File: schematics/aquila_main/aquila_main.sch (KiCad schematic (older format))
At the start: 26 parts, among them IC1 TPS62152, IC2 TPS62132

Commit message: added symbol and footprint for ADXL357
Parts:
- removed IC?: ADXL357, cusf:ADXL3x5, symbol cusf-kicad:ADXL375
- added U?: ADXL357, symbol aquila:ADXL357
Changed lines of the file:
@@
-$EndComp
-$Comp
-L cusf-kicad:ADXL375 IC?
-U 1 1 62148246
-P 6700 1700
-F 0 "IC?" H 6700 2225 50  0000 C CNN
-F 1 "ADXL357" H 6700 2134 50  0000 C CNN
-F 2 "cusf:ADXL3x5" H 6400 1000 50  0001 L CNN
-F 3 "" H 6300 1200 50  0001 C CNN
-F 4 "2361527" H 6400 900 50  0001 L CNN "Farnell"
-	1    6700 1700
-	1    0    0    -1
 $EndComp
 $Comp
@@
 Wire Wire Line
 	12700 4400 13150 4400
+$Comp
+L aquila:ADXL357 U?
+U 1 1 625041A3
+P 6600 1450
+F 0 "U?" H 6600 1475 50  0000 C CNN
+F 1 "ADXL357" H 6600 1384 50  0000 C CNN
+F 2 "" H 6600 1450 50  0001 C CNN
+F 3 "" H 6600 1450 50  0001 C CNN
+	1    6600 1450
+	1    0    0    -1
+$EndComp
 $EndSCHEMATC

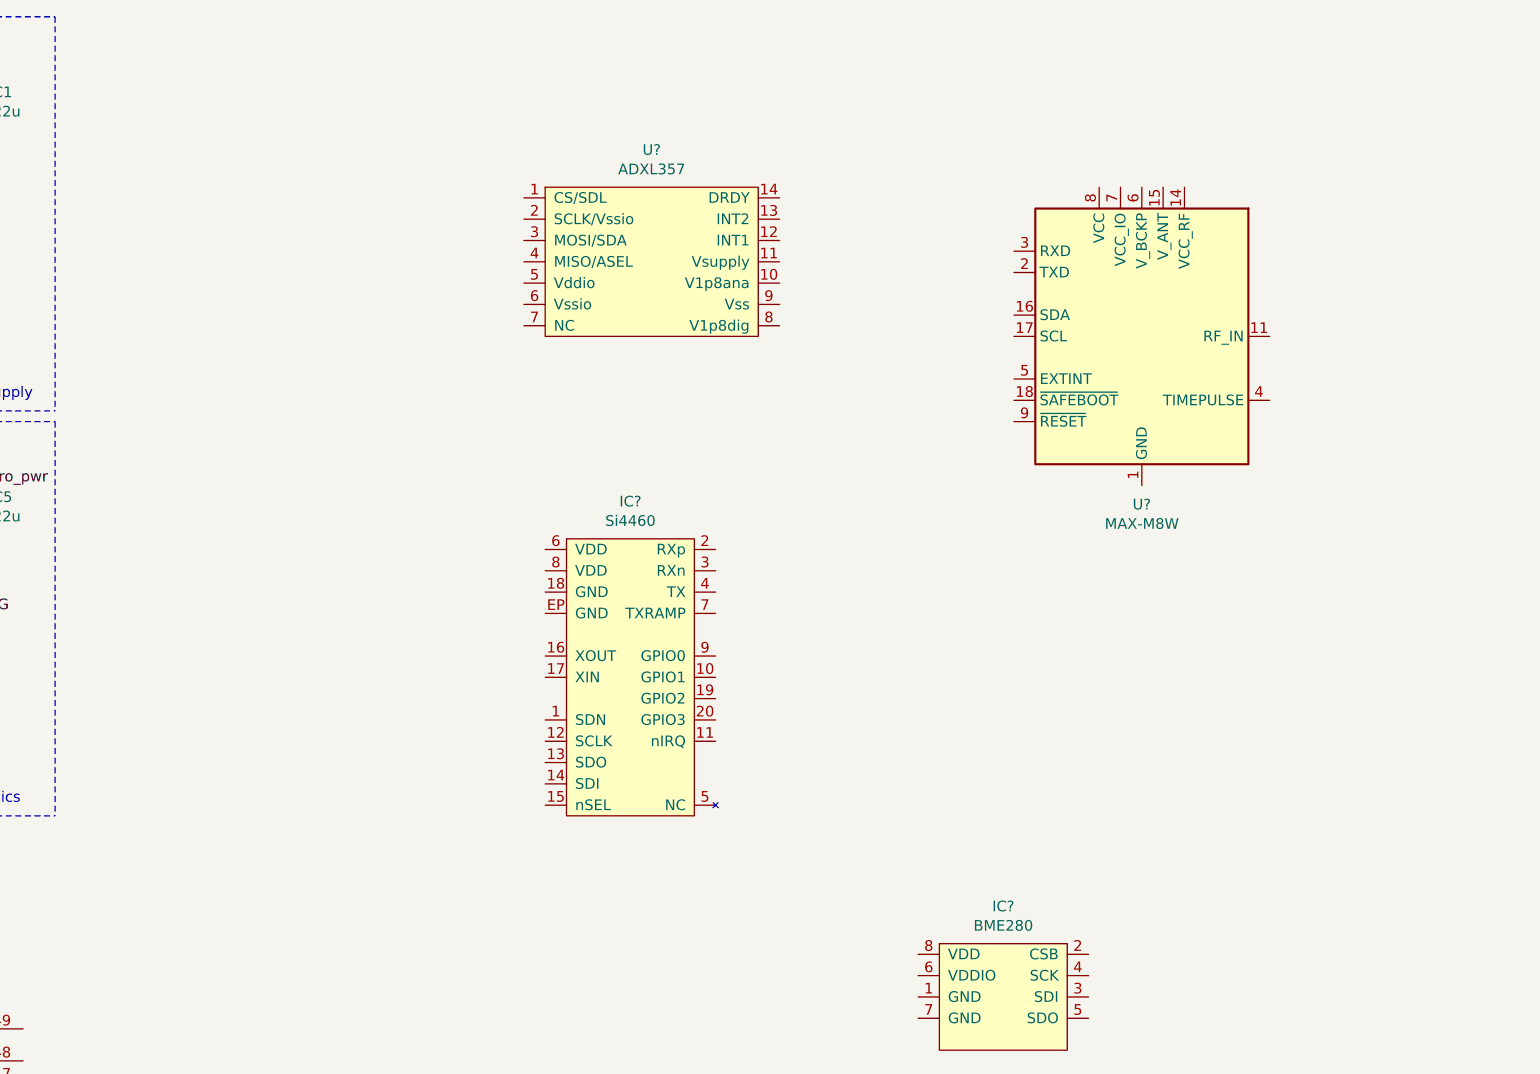
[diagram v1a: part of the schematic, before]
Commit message: added connections for accelerometer
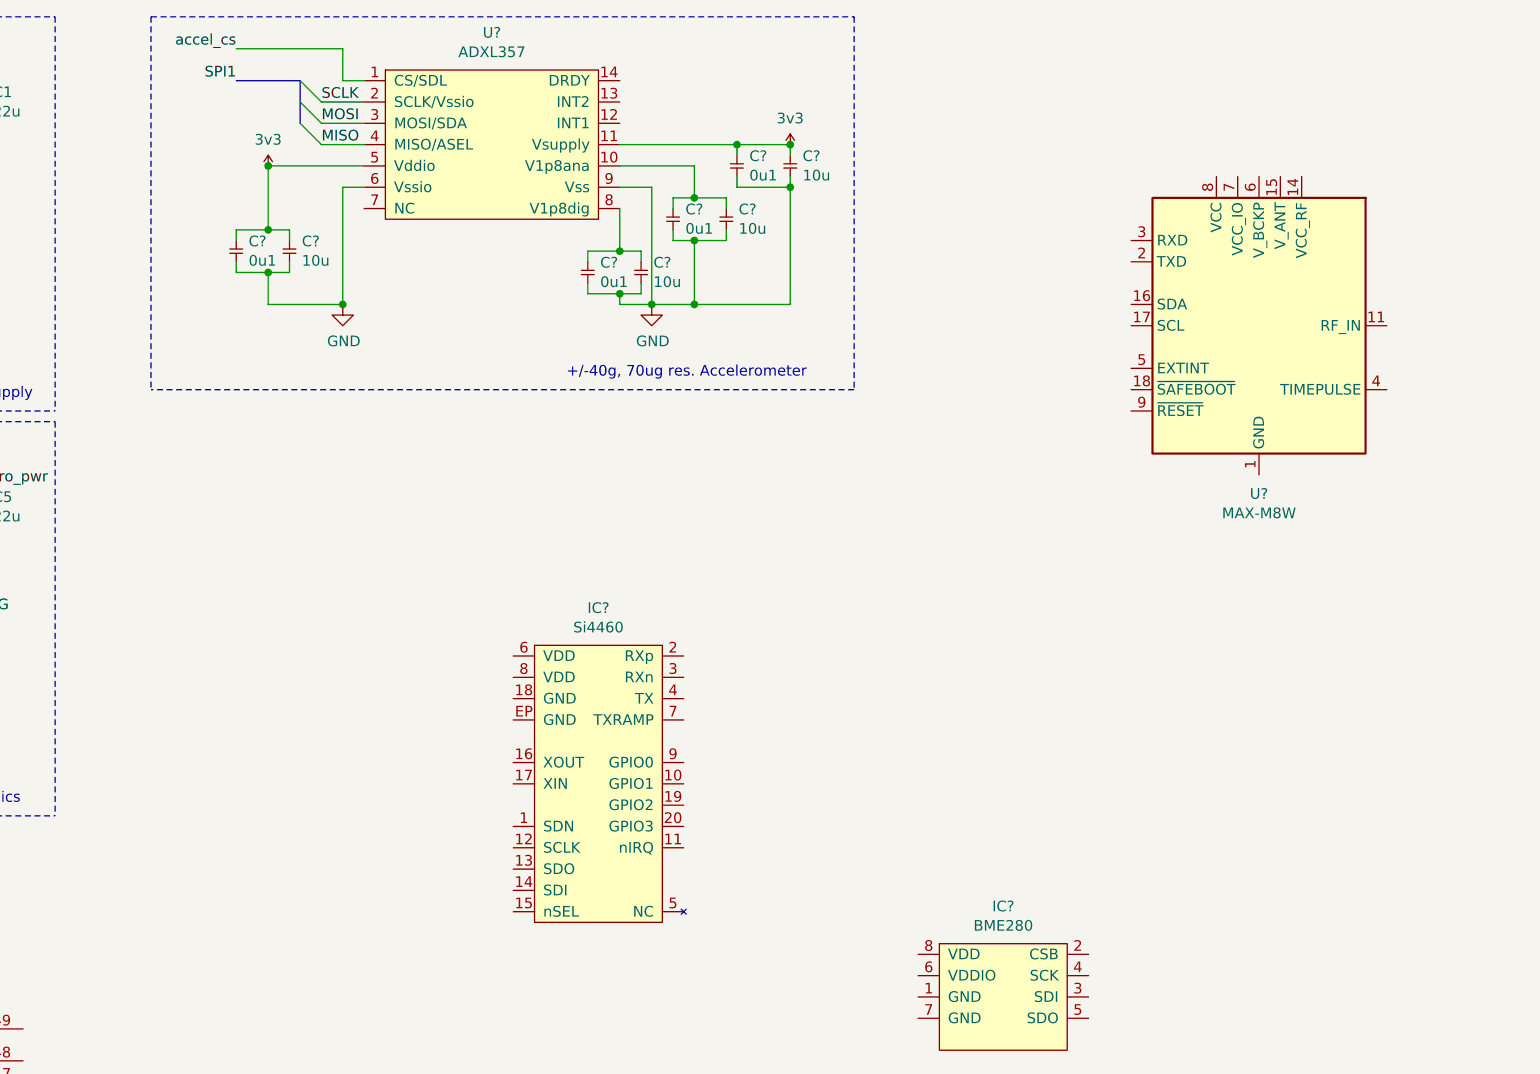
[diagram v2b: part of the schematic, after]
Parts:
- added C? (x4): 10u, symbol cusf-kicad:C
- added C? (x4): 0u1, symbol cusf-kicad:C
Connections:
- net 3v3: now also U?.11 (Vsupply), U?.5 (Vddio), C?.1, C?.1, C?.1, C?.1
- net GND: now also U?.6 (Vssio), U?.9 (Vss), C?.2, C?.2, C?.2, C?.2, C?.2, C?.2, C?.2, C?.2
- net accel_cs: now reaches U?.1 (CS/SDL)
- net at U?.10 (V1p8ana): now also C?.1, C?.1
- net SCLK: now reaches U?.2 (SCLK/Vssio)
- net MOSI: now reaches U?.3 (MOSI/SDA)
- net MISO: now reaches U?.4 (MISO/ASEL)
- net at U?.8 (V1p8dig): now also C?.1, C?.1
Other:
- note added: "+/-40g, 70ug res. Accelerometer"
- moved on the sheet: IC?, U?

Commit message: added symbol and footprint for RTC bat. holder
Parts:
- removed IC?: Si4460, cusf:QFN-20-EP-SI, symbol cusf-kicad:Si4460
- added J?: 120591-1, symbol aquila:120591-1
- added U?: Si4463, Package_DFN_QFN:QFN-20-1EP_4x4mm_P0.5mm_EP2.6x2.6mm_ThermalVias, symbol RF:Si4463
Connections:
- net GND: now also J?.2 (-), U?.18 (GND), U?.21 (GND)
- net accel_drdy: now reaches U?.14 (DRDY)
- new net vbat: J?.1 (+)
- no-connect marks 0 -> 3
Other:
- note added: "3V CR2032 for Real Time Clock"
- moved on the sheet: U?
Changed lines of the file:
@@
 L teensy:Teensy4.1 U?
 U 1 1 62144D72
-P 2550 7850
-F 0 "U?" H 2550 10415 50  0000 C CNN
-F 1 "Teensy4.1" H 2550 10324 50  0000 C CNN
-F 2 "" H 2150 8250 50  0001 C CNN
-F 3 "" H 2150 8250 50  0001 C CNN
-	1    2550 7850
-	1    0    0    -1
-$EndComp
-$Comp
-L cusf-kicad:Si4460 IC?
-U 1 1 62148F07
-P 6350 4400
-F 0 "IC?" H 6350 5225 50  0000 C CNN
-F 1 "Si4460" H 6350 5134 50  0000 C CNN
-F 2 "cusf:QFN-20-EP-SI" H 6050 3600 50  0001 L CNN
-F 3 "" H 5950 5000 50  0001 C CNN
-F 4 "2462635" H 6050 3500 50  0001 L CNN "Farnell"
-	1    6350 4400
+P 2750 9200
+F 0 "U?" H 2750 11765 50  0000 C CNN
+F 1 "Teensy4.1" H 2750 11674 50  0000 C CNN
+F 2 "" H 2350 9600 50  0001 C CNN
+F 3 "" H 2350 9600 50  0001 C CNN
+	1    2750 9200
 	1    0    0    -1
 $EndComp
@@
 Wire Notes Line
 	4250 800  4250 2550
+NoConn ~ 5250 1700
+NoConn ~ 6450 1200
+NoConn ~ 6450 1300
+Text Label 6700 1100 0    50   ~ 0
+accel_drdy
+Wire Wire Line
+	6450 1100 6700 1100
+$Comp
+L RF:Si4463 U?
+U 1 1 6268F7FD
+P 5300 4400
+F 0 "U?" H 5300 5400 50  0000 C CNN
+F 1 "Si4463" H 5300 5300 50  0000 C CNN
+F 2 "Package_DFN_QFN:QFN-20-1EP_4x4mm_P0.5mm_EP2.6x2.6mm_ThermalVias" H 5300 5600 50  0001 C CNN
+F 3 "https://www.silabs.com/documents/public/data-sheets/Si4464-63-61-60.pdf" H 5000 4300 50  0001 C CNN
+	1    5300 4400
+	1    0    0    -1
+$EndComp
+$Comp
+L aquila:120591-1 J?
+U 1 1 626A7BFD
+P 1550 4650
+F 0 "J?" H 1678 4526 50  0000 L CNN
+F 1 "120591-1" H 1678 4435 50  0000 L CNN
+F 2 "" H 1550 4800 50  0001 C CNN
+F 3 "" H 1550 4800 50  0001 C CNN
+	1    1550 4650
+	1    0    0    -1
+$EndComp
+Wire Wire Line
+	1400 4900 1400 5000
+$Comp
+L power:GND #PWR?
+U 1 1 626ADD67
+P 1400 5000
+F 0 "#PWR?" H 1400 4750 50  0001 C CNN
+F 1 "GND" H 1405 4827 50  0000 C CNN
+F 2 "" H 1400 5000 50  0001 C CNN
+F 3 "" H 1400 5000 50  0001 C CNN
+	1    1400 5000
+	1    0    0    -1
+$EndComp
+Text Label 1250 4750 2    50   ~ 0
+vbat
+Wire Wire Line
+	1250 4750 1400 4750
+Wire Notes Line
+	1000 4600 3800 4600
+Wire Notes Line
+	1000 5300 3800 5300
+Wire Notes Line
+	1000 4600 1000 5300
+Wire Notes Line
+	3800 4600 3800 5300
 Wire Bus Line
 	4950 1100 4950 1300
+Text Notes 2550 5250 0    50   ~ 0
+3V CR2032 for Real Time Clock
 $EndSCHEMATC

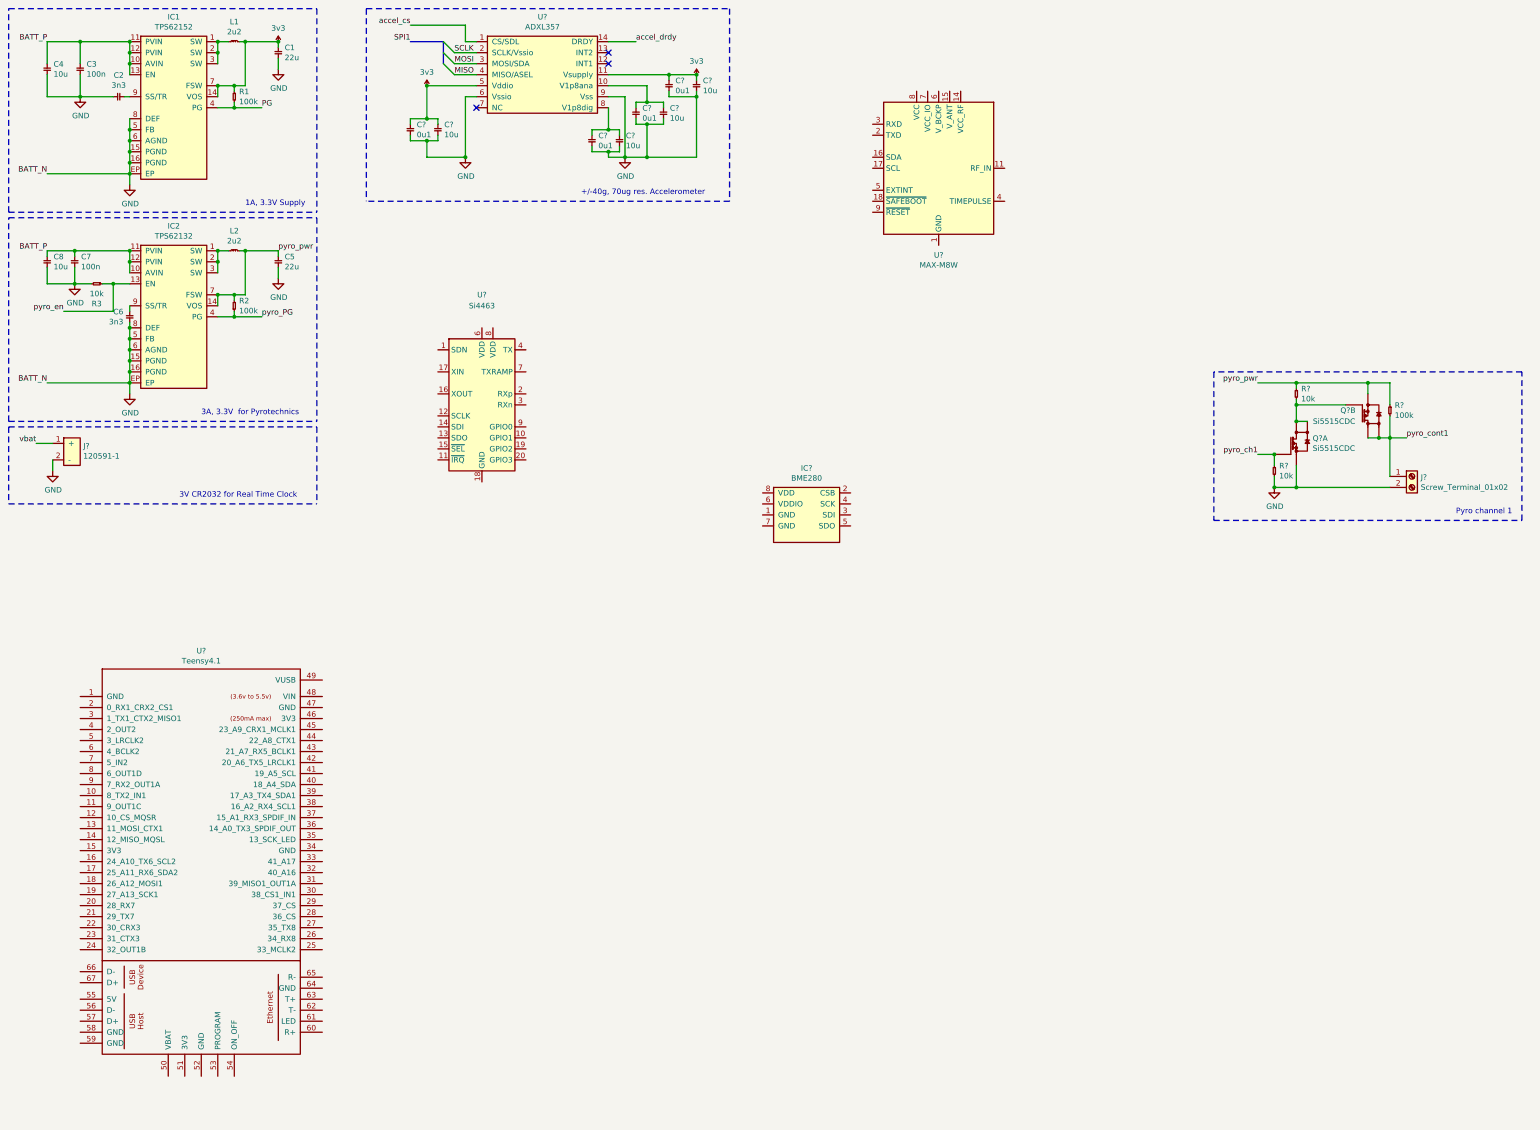
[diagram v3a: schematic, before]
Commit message: added connections for barometer
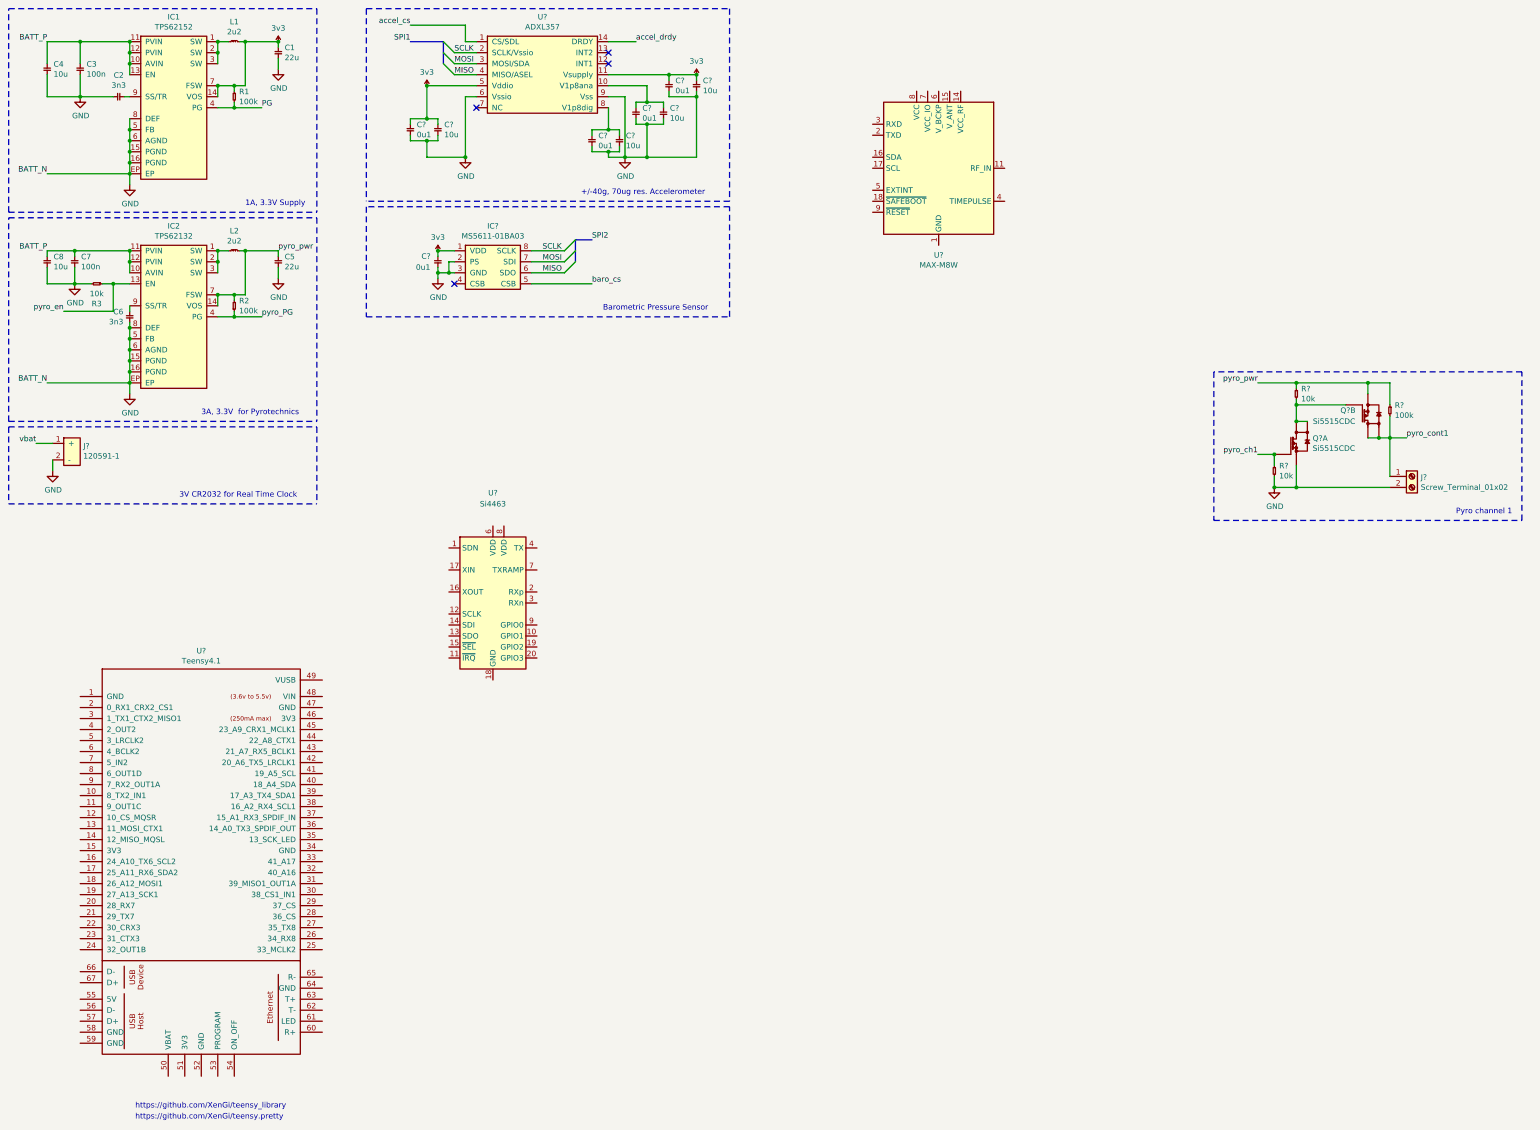
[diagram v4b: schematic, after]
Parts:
- removed IC?: BME280, cusf:BME280, symbol cusf-kicad:BME280
- added C?: 0u1, symbol cusf-kicad:C
- added IC?: MS5611-01BA03, cusf:MS5611, symbol cusf-kicad:MS5611-01BA03
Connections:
- net 3v3: now also C?.1, IC?.1 (VDD)
- net GND: now also C?.2, IC?.2 (PS), IC?.3 (GND)
- net MISO: now also IC?.6 (SDO)
- net MOSI: now also IC?.7 (SDI)
- net SCLK: now also IC?.8 (SCLK)
- new net baro_cs: IC?.5 (CSB)
- no-connect marks 3 -> 4
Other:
- note added: "Barometric Pressure Sensor"
- note added: "https://github.com/XenGi/teensy.pretty"
- note added: "https://github.com/XenGi/teensy_library"
- moved on the sheet: U?
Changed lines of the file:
@@
 	2100 2300 1350 2300
-$Comp
-L cusf-kicad:BME280 IC?
-U 1 1 621D3869
-P 8250 5400
-F 0 "IC?" H 8250 5825 50  0000 C CNN
-F 1 "BME280" H 8250 5734 50  0000 C CNN
-F 2 "cusf:BME280" H 7950 5000 50  0001 L CNN
-F 3 "https://ae-bst.resource.bosch.com/media/_tech/media/datasheets/BST-BME280_DS001-11.pdf" H 7950 4900 50  0001 L CNN
-F 4 "262-BME280" H 7950 4800 50  0001 L CNN "Mouser"
-F 5 "828-1063-1-ND" H 7950 4700 50  0001 L CNN "Digi-Key"
-	1    8250 5400
-	1    0    0    -1
-$EndComp
 $Comp
 L cusf-kicad:3v3 #PWR?
@@
 L RF:Si4463 U?
 U 1 1 6268F7FD
-P 5300 4400
-F 0 "U?" H 5300 5400 50  0000 C CNN
-F 1 "Si4463" H 5300 5300 50  0000 C CNN
-F 2 "Package_DFN_QFN:QFN-20-1EP_4x4mm_P0.5mm_EP2.6x2.6mm_ThermalVias" H 5300 5600 50  0001 C CNN
-F 3 "https://www.silabs.com/documents/public/data-sheets/Si4464-63-61-60.pdf" H 5000 4300 50  0001 C CNN
-	1    5300 4400
+P 5400 6200
+F 0 "U?" H 5400 7200 50  0000 C CNN
+F 1 "Si4463" H 5400 7100 50  0000 C CNN
+F 2 "Package_DFN_QFN:QFN-20-1EP_4x4mm_P0.5mm_EP2.6x2.6mm_ThermalVias" H 5400 7400 50  0001 C CNN
+F 3 "https://www.silabs.com/documents/public/data-sheets/Si4464-63-61-60.pdf" H 5100 6100 50  0001 C CNN
+	1    5400 6200
 	1    0    0    -1
 $EndComp
@@
 F 1 "120591-1" H 1678 4435 50  0000 L CNN
 F 2 "" H 1550 4800 50  0001 C CNN
-F 3 "" H 1550 4800 50  0001 C CNN
+F 3 "https://www.farnell.com/cad/1815976.pdf" H 1550 4800 50  0001 C CNN
 	1    1550 4650
 	1    0    0    -1
@@
 Wire Notes Line
 	3800 4600 3800 5300
+Text Notes 2550 5250 0    50   ~ 0
+3V CR2032 for Real Time Clock
+Text Notes 2150 10800 0    50   ~ 0
+https://github.com/XenGi/teensy_library
+Text Notes 2150 10900 0    50   ~ 0
+https://github.com/XenGi/teensy.pretty
+$Comp
+L cusf-kicad:3v3 #PWR?
+U 1 1 622BAFBF
+P 4900 3000
+F 0 "#PWR?" H 4900 3110 50  0001 L CNN
+F 1 "3v3" H 4900 3123 50  0000 C CNN
+F 2 "" H 4900 3000 50  0001 C CNN
+F 3 "" H 4900 3000 50  0001 C CNN
+	1    4900 3000
+	1    0    0    -1
+$EndComp
+Wire Wire Line
+	5050 3000 4900 3000
+$Comp
+L cusf-kicad:MS5611-01BA03 IC?
+U 1 1 622B2C48
+P 5350 3100
+F 0 "IC?" H 5400 3425 50  0000 C CNN
+F 1 "MS5611-01BA03" H 5400 3334 50  0000 C CNN
+F 2 "cusf:MS5611" H 5150 2700 50  0001 L CNN
+F 3 "" H 5400 3100 50  0001 C CNN
+F 4 "2362662" H 5150 2600 50  0001 L CNN "Farnell"
+	1    5350 3100
+	1    0    0    -1
+$EndComp
+NoConn ~ 5050 3300
+$Comp
+L power:GND #PWR?
+U 1 1 622FE465
+P 4900 3250
+F 0 "#PWR?" H 4900 3000 50  0001 C CNN
+F 1 "GND" H 4905 3077 50  0000 C CNN
+F 2 "" H 4900 3250 50  0001 C CNN
+F 3 "" H 4900 3250 50  0001 C CNN
+	1    4900 3250
+	1    0    0    -1
+$EndComp
+Wire Wire Line
+	5050 3200 5000 3200
+Wire Wire Line
+	4900 3200 4900 3250
+Wire Wire Line
+	5050 3100 5000 3100
+Wire Wire Line
+	5000 3100 5000 3200
+Connection ~ 5000 3200
+Wire Wire Line
+	5000 3200 4900 3200
+$Comp
+L cusf-kicad:C C?
+U 1 1 62311113
+P 4900 3050
+F 0 "C?" V 4900 2900 50  0000 L CNN
+F 1 "0u1" V 5000 2850 50  0000 L CNN
+F 2 "" H 4900 3050 50  0001 C CNN
+F 3 "" H 4900 3050 50  0001 C CNN
+	1    4900 3050
+	0    1    1    0
+$EndComp
+Wire Wire Line
+	4900 3000 4900 3050
+Connection ~ 4900 3000
+Wire Wire Line
+	4900 3150 4900 3200
+Connection ~ 4900 3200
+Entry Wire Line
+	6050 3000 6150 2900
+Entry Wire Line
+	6050 3100 6150 3000
+Entry Wire Line
+	6050 3200 6150 3100
+Wire Bus Line
+	6150 2900 6300 2900
+Wire Wire Line
+	6050 3000 5750 3000
+Wire Wire Line
+	5750 3100 6050 3100
+Wire Wire Line
+	6050 3200 5750 3200
+Text Label 5850 3000 0    50   ~ 0
+SCLK
+Text Label 5850 3100 0    50   ~ 0
+MOSI
+Text Label 5850 3200 0    50   ~ 0
+MISO
+Text Label 6300 2900 0    50   ~ 0
+SPI2
+Wire Wire Line
+	5750 3300 6300 3300
+Text Label 6300 3300 0    50   ~ 0
+baro_cs
+Wire Notes Line
+	4250 2600 4250 3600
+Wire Notes Line
+	4250 3600 7550 3600
+Wire Notes Line
+	7550 3600 7550 2600
+Wire Notes Line
+	7550 2600 4250 2600
 Wire Bus Line
 	4950 1100 4950 1300
-Text Notes 2550 5250 0    50   ~ 0
-3V CR2032 for Real Time Clock
+Wire Bus Line
+	6150 2900 6150 3100
+Text Notes 6400 3550 0    50   ~ 0
+Barometric Pressure Sensor
 $EndSCHEMATC
